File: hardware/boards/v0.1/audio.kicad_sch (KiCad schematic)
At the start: 30 parts, among them J10 MIDI_IN, J11 MIDI_OUT, J6 HP, J8 LINE_OUT, J9 LINE_IN, U24 MIC, U28 TS5A23159RSE, U29 NAU88C22YG

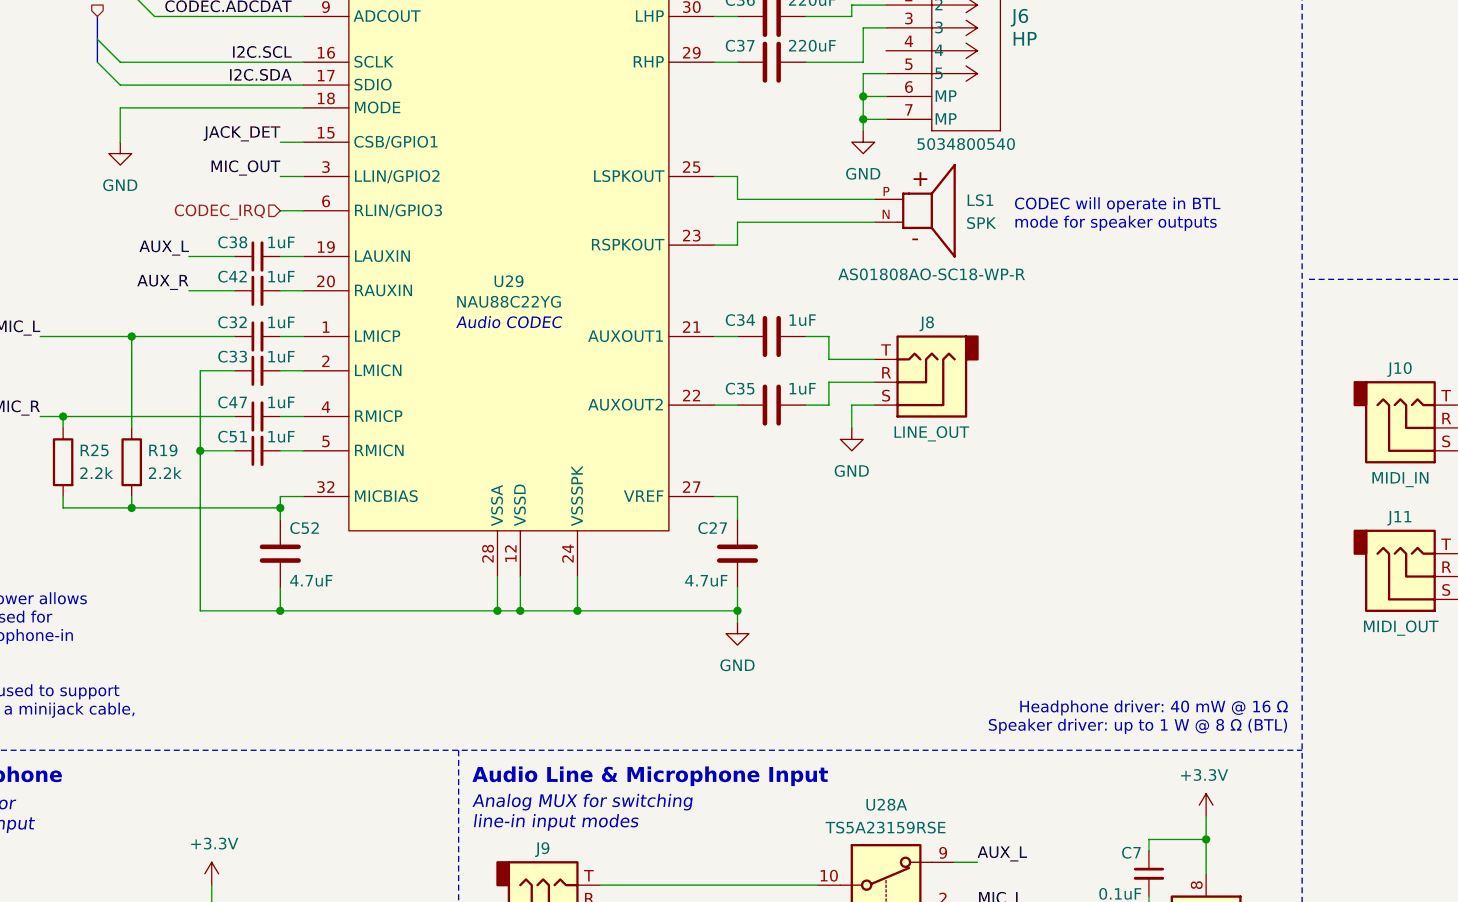
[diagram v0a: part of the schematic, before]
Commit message: feat: various component and layout changes
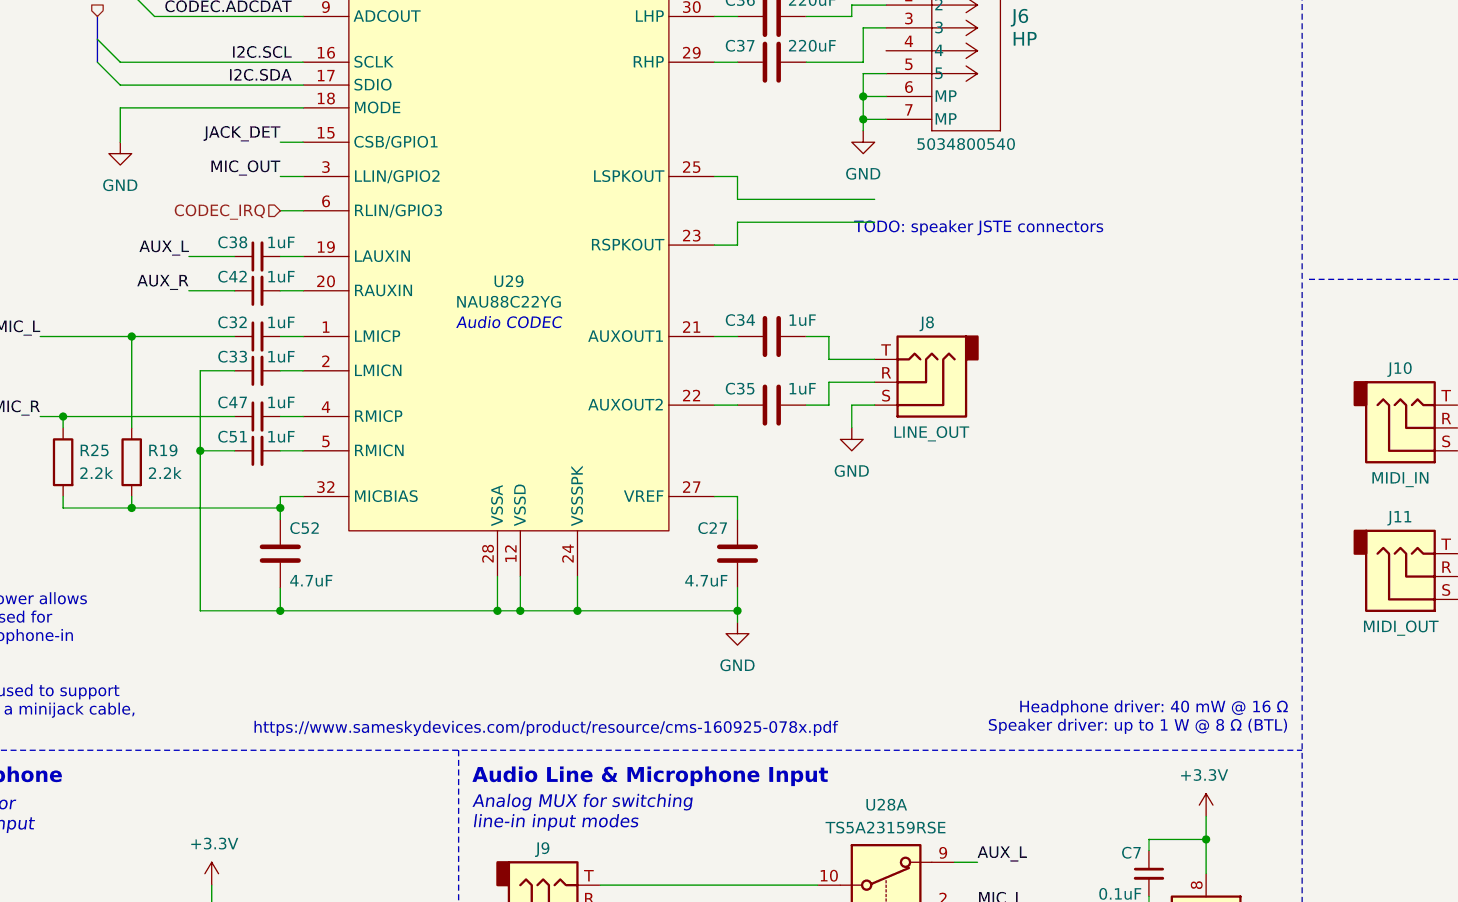
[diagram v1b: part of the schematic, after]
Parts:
- removed LS1: SPK, pocket_synth:AS01808AO-SC18-WP-R, symbol pocket_synth:AS01808AO-SC18-WP-R
- J10, J11, J8, J9: footprint Connector_Audio:Jack_3.5mm_CUI_SJ-3523-SMT_Horizontal -> rhais_connector-lumberg:1503-02
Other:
- note added: "TODO: speaker JSTE connectors"
- note added: "https://www.sameskydevices.com/product/resource/cms-160925-078x.pdf"
- note removed: "CODEC will operate in BTL mode for speaker outputs"

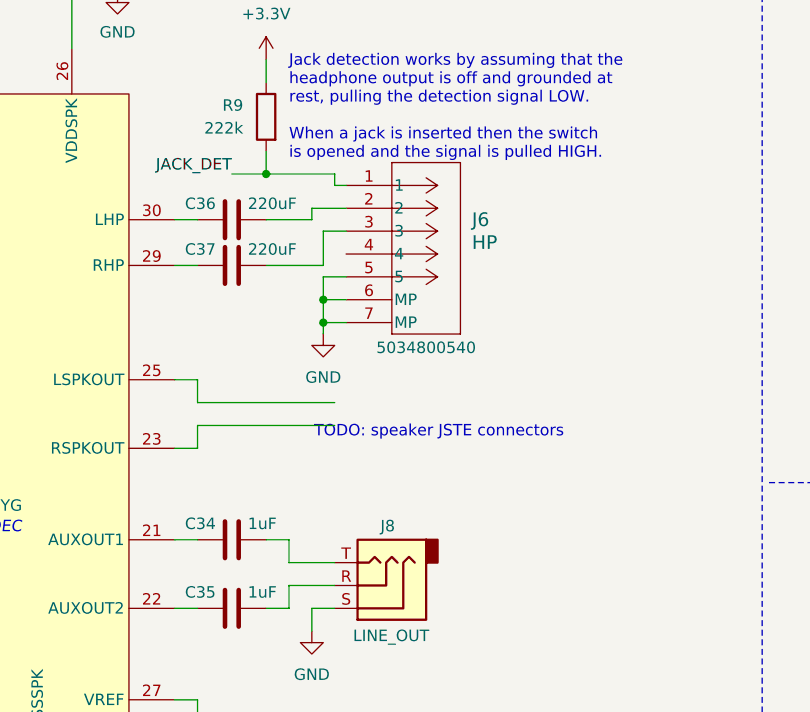
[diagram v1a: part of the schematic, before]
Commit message: feat: add menu buttons and speaker connectors
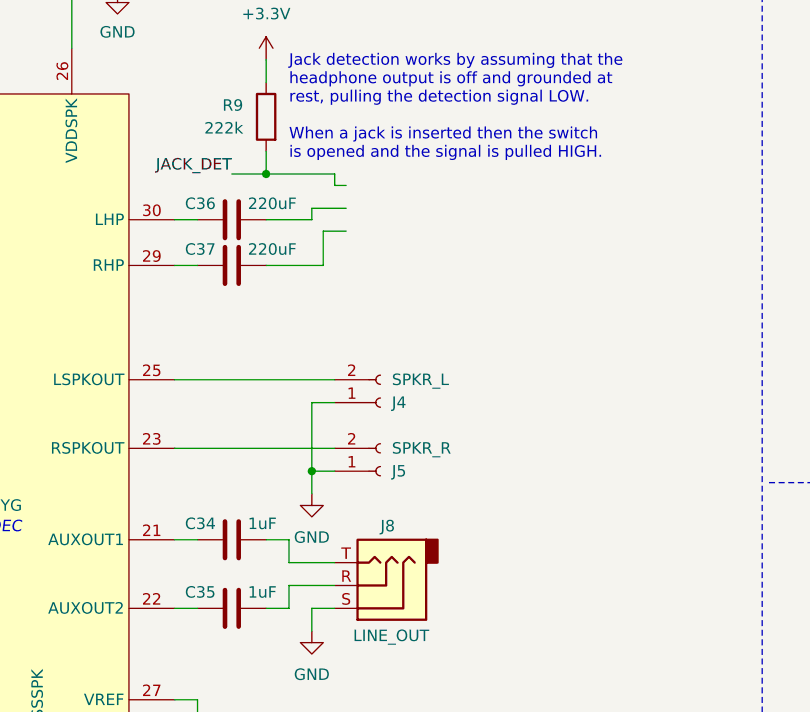
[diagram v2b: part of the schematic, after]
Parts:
- removed J6: HP, pocket_synth:CONN_503480-0540_MOL, symbol pocket_synth:5034800540
- added J4: SPKR_L, pocket_synth:MOLEX_532610271, symbol Connector:Conn_01x02_Socket
- added J5: SPKR_R, pocket_synth:MOLEX_532610271, symbol Connector:Conn_01x02_Socket
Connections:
- net GND: now also J4.1 (Pin_1), J5.1 (Pin_1)
- net at U29.23 (RSPKOUT): now also J5.2 (Pin_2)
- net at U29.25 (LSPKOUT): now also J4.2 (Pin_2)
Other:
- note removed: "TODO: speaker JSTE connectors"

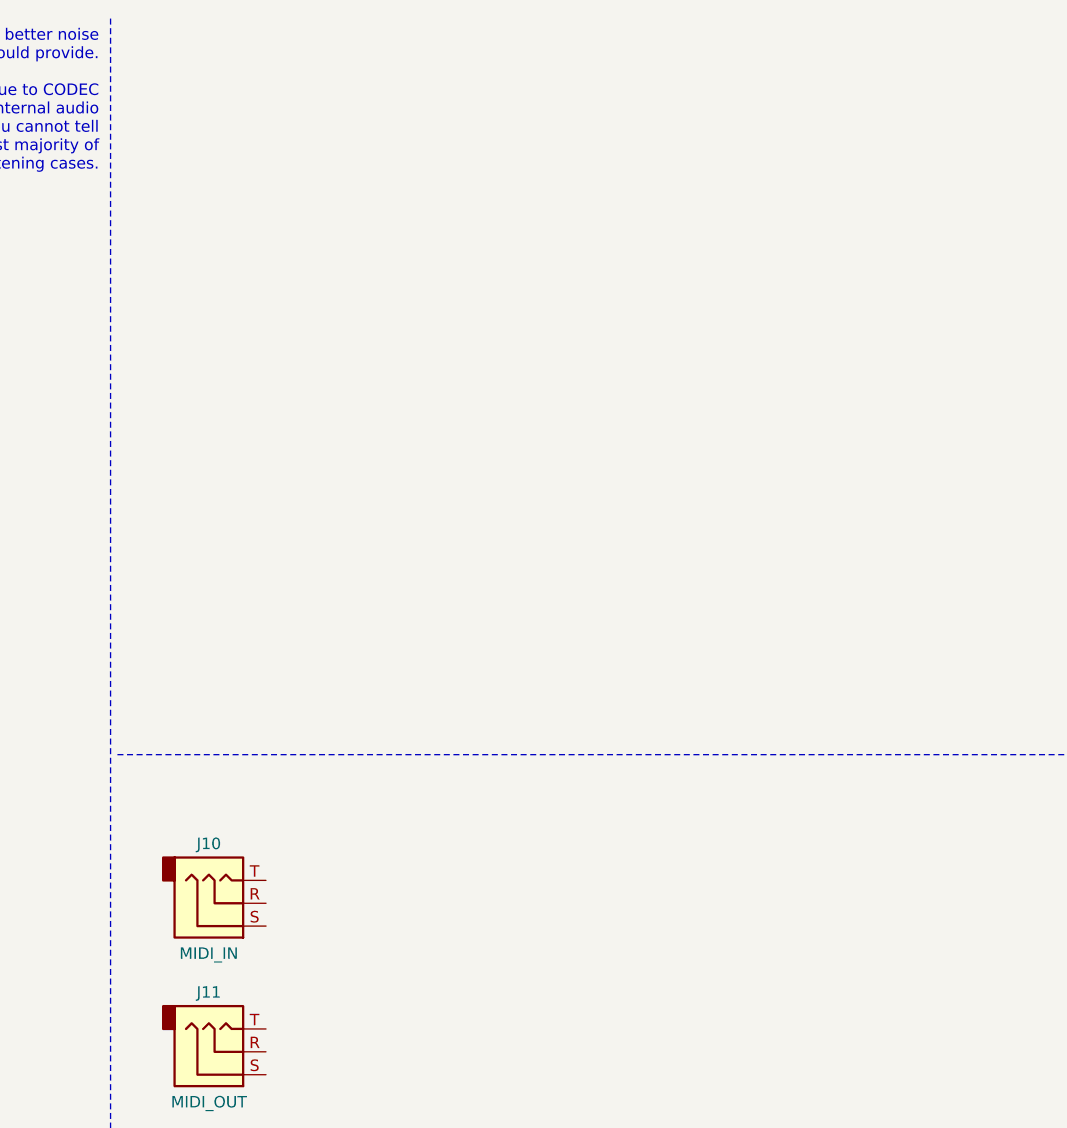
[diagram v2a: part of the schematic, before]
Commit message: feat: schematic organization
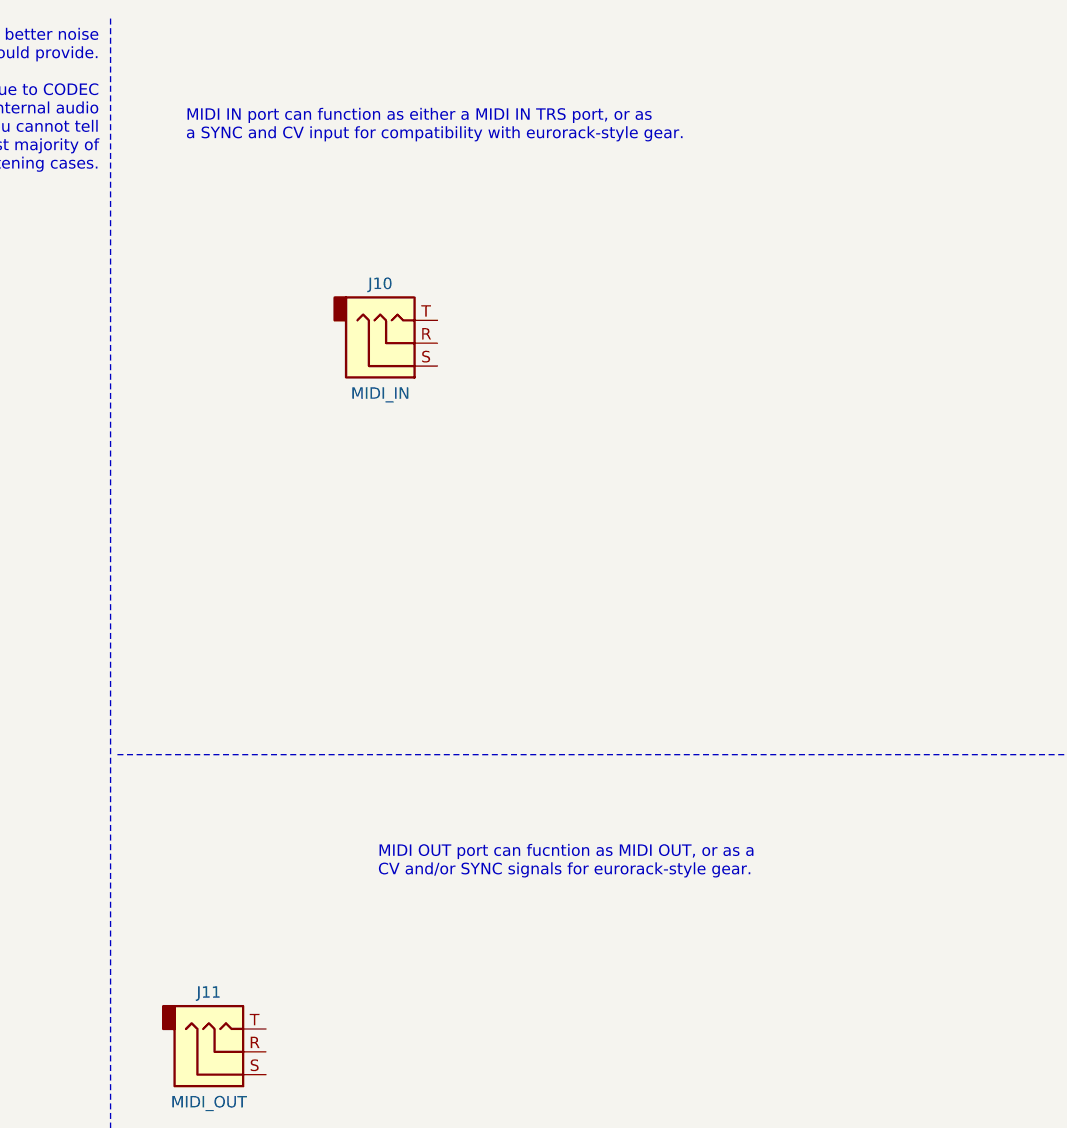
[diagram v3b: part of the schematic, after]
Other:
- note added: "MIDI IN port can function as either a MIDI IN TRS port, or as a SYNC and CV input for compatibility with eurorack-style gear."
- note added: "MIDI OUT port can fucntion as MIDI OUT, or as a CV and/or SYNC signals for eurorack-style gear."
- moved on the sheet: J10
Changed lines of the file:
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@@
 		)
 	)
+	(text "MIDI OUT port can fucntion as MIDI OUT, or as a\nCV and/or SYNC signals for eurorack-style gear."
+		(exclude_from_sim no)
+		(at 206.756 104.14 0)
+		(effects
+			(font
+				(size 1.27 1.27)
+				(color 132 132 132 1)
+			)
+			(justify left top)
+		)
+	)
 	(text "ADC is recorded at 24-bit for a better noise\nfloor then recording at 16-bit would provide. \n\nPlayback is done at 24-bit due to CODEC\nrestrictions, however the internal audio\nengine runs in 16-bit as you cannot tell\nthe difference in the vast majority of \nlistening cases."
 		(exclude_from_sim no)
@@
 		)
 	)
+	(text "MIDI IN port can function as either a MIDI IN TRS port, or as \na SYNC and CV input for compatibility with eurorack-style gear. "
+		(exclude_from_sim no)
+		(at 185.42 22.352 0)
+		(effects
+			(font
+				(size 1.27 1.27)
+				(color 132 132 132 1)
+			)
+			(justify left top)
+		)
+	)
 	(junction
 		(at 73.66 39.37)
@@
 	(symbol
 		(lib_id "Connector_Audio:AudioJack3")
-		(at 189.23 110.49 0)
+		(at 208.28 48.26 0)
 		(mirror x)
 		(unit 1)
@@
 		(dnp no)
 		(property "Reference" "J10"
-			(at 187.96 103.886 0)
+			(at 207.01 41.656 0)
 			(effects
 				(font
@@
 		)
 		(property "Value" "MIDI_IN"
-			(at 187.96 116.078 0)
+			(at 207.01 53.848 0)
 			(effects
 				(font
@@
 		)
 		(property "Footprint" "rhais_connector-lumberg:1503-02"
-			(at 189.23 110.49 0)
+			(at 208.28 48.26 0)
 			(effects
 				(font
@@
 		)
 		(property "Datasheet" "~"
-			(at 189.23 110.49 0)
+			(at 208.28 48.26 0)
 			(effects
 				(font
@@
 		)
 		(property "Description" "Audio Jack, 3 Poles (Stereo / TRS)"
-			(at 189.23 110.49 0)
+			(at 208.28 48.26 0)
 			(effects
 				(font
@@
 		)
 		(property "JLC" "C4991872"
-			(at 189.23 110.49 0)
+			(at 208.28 48.26 0)
 			(effects
 				(font
@@
 		)
 		(property "Arrow Part Number" ""
-			(at 189.23 110.49 0)
+			(at 208.28 48.26 0)
 			(effects
 				(font
@@
 		)
 		(property "Arrow Price/Stock" ""
-			(at 189.23 110.49 0)
+			(at 208.28 48.26 0)
 			(effects
 				(font
@@
 		)
 		(property "MANUFACTURER" ""
-			(at 189.23 110.49 0)
+			(at 208.28 48.26 0)
 			(effects
 				(font
@@
 		)
 		(property "MAXIMUM_PACKAGE_HEIGHT" ""
-			(at 189.23 110.49 0)
+			(at 208.28 48.26 0)
 			(effects
 				(font
@@
 		)
 		(property "PARTREV" ""
-			(at 189.23 110.49 0)
+			(at 208.28 48.26 0)
 			(effects
 				(font
@@
 		)
 		(property "STANDARD" ""
-			(at 189.23 110.49 0)
+			(at 208.28 48.26 0)
 			(effects
 				(font
